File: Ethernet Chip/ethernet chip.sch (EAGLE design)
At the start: 28 parts

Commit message: Updated Ethernet Chip Schematic
10/31/15 5:48
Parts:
- added U$1: LAN8720LAN8720, Luke:LAN8720LAN8720
- added U$2: J00-0065NL, Paul's Library:J00-0065NL
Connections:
- new net AECRSDV: R3.1
- new net AEMDE: U$1.MDC
- new net AEMDIO: U$1.MDIO
- new net AEREFCLK: R4.1
- new net AERXD1: R2.1
- new net AERXDO: R1.1
- new net AERXERR: U$1.RXER/PHYAD0
- new net AETXD0: R6.1
- new net AETXD1: R7.1
- new net AETXEN: R5.1
- new net BUS_SPEED: R18.2, U$1.LED2/NINTSEL, U$2.G_GND
- new net CT1: C10.1, C5.2, C6.2, C7.1, C8.1, C9.1, R12.2, R13.2, R14.2, R15.2, U$2.CT1, U$2.CT2
- new net G: R16.1, U$2.G
- new net LINK/ACT: U$1.LED1/REGOFF, U$2.Y
- new net N$1: R1.2, U$1.RXD0/MODE0
- new net N$10: R7.2, U$1.TXD1
- new net N$11: R11.1, U$1.VDD1A, U$1.VDD2A
- new net N$13: C2.1, R9.1, U$1.XTAL1/CLKIN
- new net N$14: U$1.NRST
- new net N$18: R17.1, U$2.Y_GND
- new net N$2: R2.2, U$1.RXD1/MODE1
- new net N$5: R3.2, U$1.CRS_DV/MODE2
- new net N$7: R4.2, U$1.NINT/REFCLKO
- new net N$8: R5.2, U$1.TXEN
- new net N$9: R6.2, U$1.TXD0
- new net RD+: R14.1, U$1.RXP, U$2.RD+
- new net RD-: R15.1, U$1.RXN, U$2.RD-
- new net TD+: R12.1, U$1.TXP, U$2.TD+
- new net TD-: R13.1, U$1.TXN, U$2.TD-
- net +3V3: now also U$1.VDDIO; no longer C10.1, C5.2, C6.2, C7.1, C8.1, C9.1, R12.2, R13.2, R14.2, R15.2
- net GND: now also U$1.VSS_PAD, U$2.GND
- net N$3: now also U$1.VDDCR
- net N$4: now also R10.1, U$1.RBIAS; no longer C2.1, R9.1
- net N$6: now also U$1.XTAL2

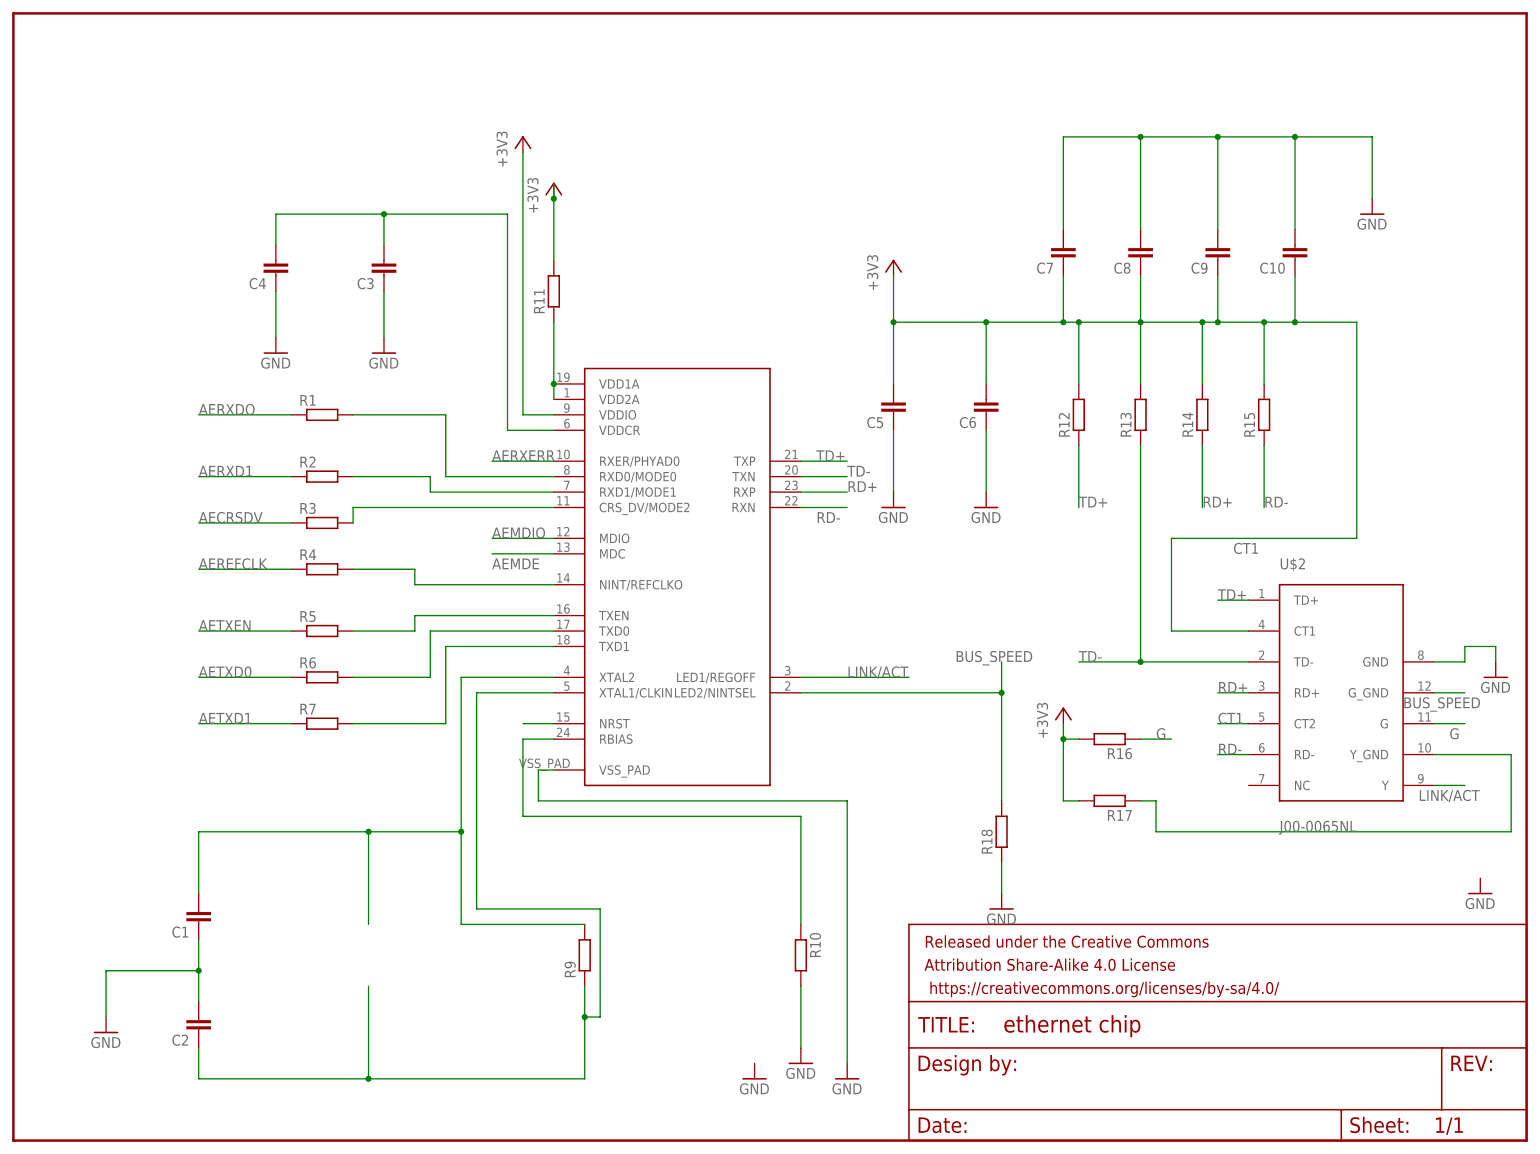
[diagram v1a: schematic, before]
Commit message: Updated Ethernet Chip Schematic
11/4/15
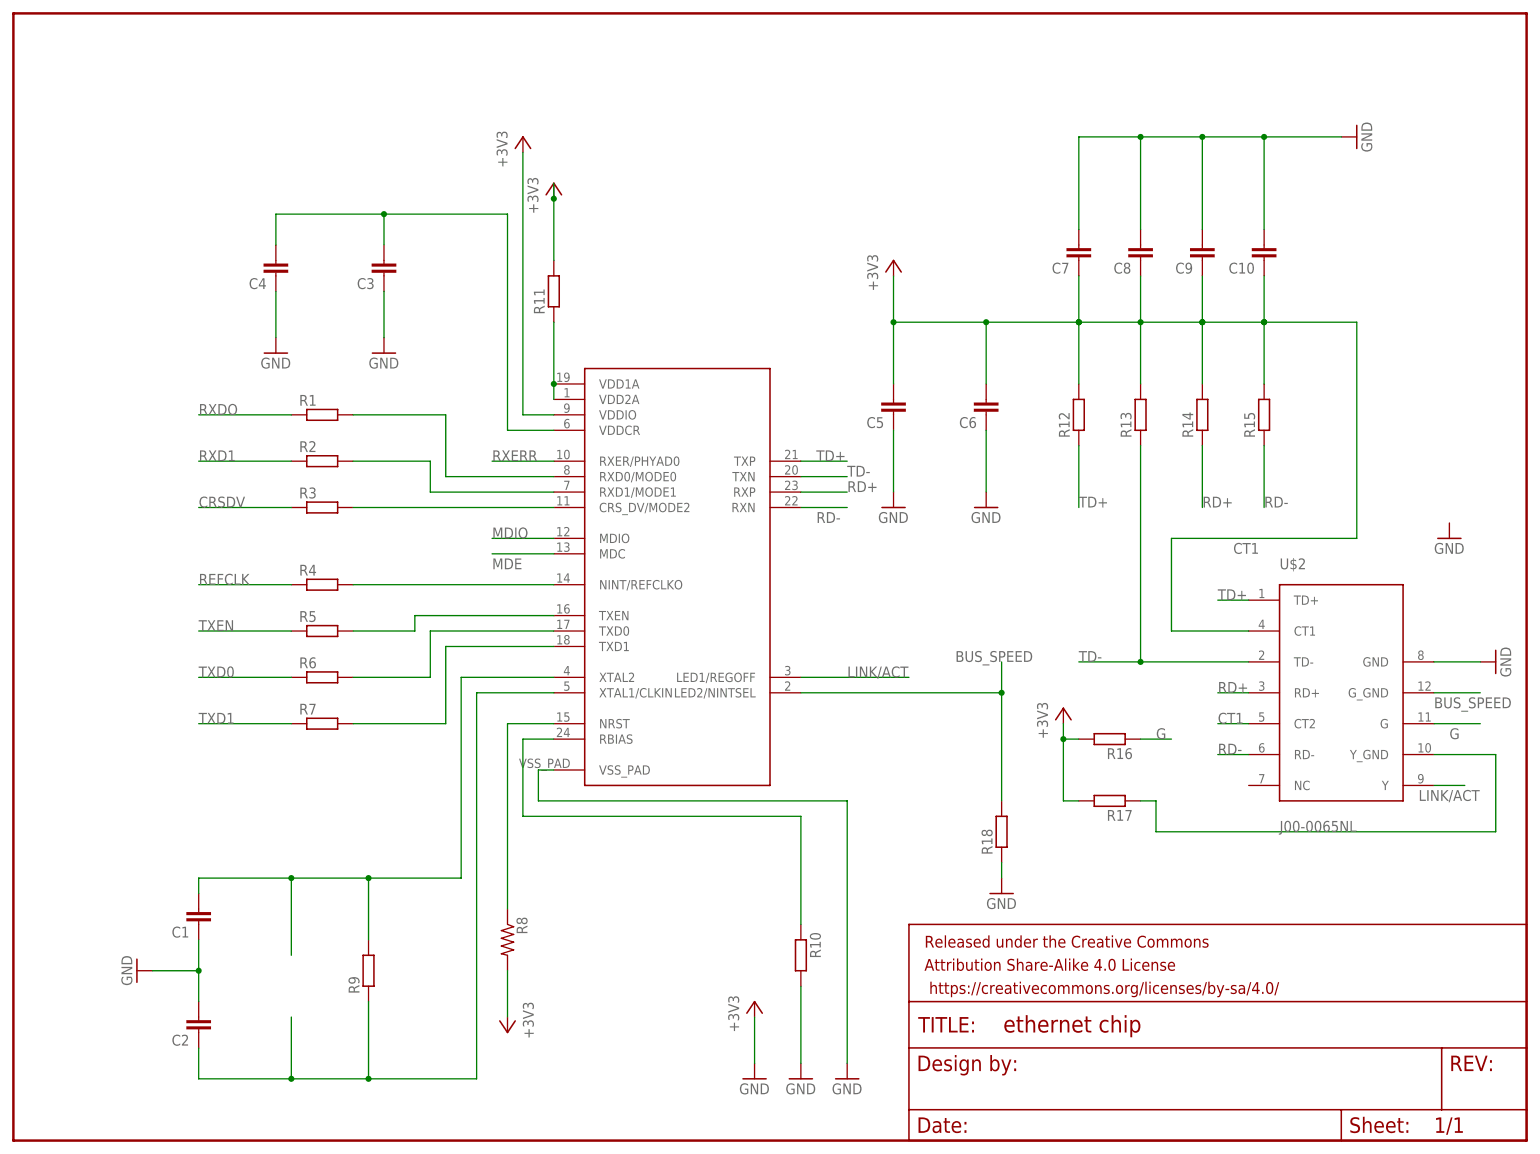
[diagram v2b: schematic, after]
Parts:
- added R8: (no value), SparkFun-Passives:RESISTOR0603-RES
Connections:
- net AECRSDV renamed CRSDV
- net AEMDE renamed MDE
- net AEMDIO renamed MDIO
- net AEREFCLK renamed REFCLK
- net AERXD1 renamed RXD1
- net AERXDO renamed RXDO
- net AERXERR renamed RXERR
- net AETXD0 renamed TXD0
- net AETXD1 renamed TXD1
- net AETXEN renamed TXEN
- net +3V3: now also R8.2
- net N$14: now also R8.1
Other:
- moved on the sheet: C10, C7, C9, R2, R3, R4, R9
